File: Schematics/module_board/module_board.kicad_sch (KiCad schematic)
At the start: 33 parts, among them J1 Conn_01x01_Male, J11 Conn_01x01_Male, J12 Conn_01x01_Male, J13 Conn_01x01_Male, J14 Conn_01x01_Male, J15 Conn_01x01_Male, J16 Conn_01x01_Male, J17 Conn_01x01_Male, J2 Conn_01x01_Male, J3 Conn_01x01_Male, J4 Conn_01x01_Male, J5 Conn_01x06_Male, U1 RP2040, U2 W25Q16JVSSIQ, Y1 ABLS-12.000MHZ-B4-T

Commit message: Update project symbol table
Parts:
- removed U2: W25Q16JVSSIQ, Package_SO:SOIC-8_5.23x5.23mm_P1.27mm, symbol Merrick_Symbols_KiCad6:W25Q16JVSSIQ
- added U?: W25Q16JVSSIQ, symbol prototroller_symbols:W25Q16JVSSIQ
- J5: footprint Prototroller:Mag_Pogo_6P_P2.2mm_Male -> prototroller_footprints:Mag_Pogo_6P_P2.2mm_Male
- Y1: footprint ABLS-12:XTAL_ABLS-12.000MHZ-B4-T -> prototroller_footprints:XTAL_ABLS-12.000MHZ-B4-T
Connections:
- net +3V3: now also U?.8 (VCC)
- net GND: now also U?.4 (GND)
- net QSPI_NSS: now also U?.1 (~{CS})
- net QSPI_SCLK: now also U?.6 (CLK)
- net QSPI_SD0: now also U?.5 (DI(IO0))
- net QSPI_SD1: now also U?.2 (DO(IO1))
- net QSPI_SD2: now also U?.3 (IO2)
- net QSPI_SD3: now also U?.7 (IO3)
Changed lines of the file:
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@@
       (effects (font (size 1.27 1.27)) (justify right))
     )
-    (property "Footprint" "ABLS-12:XTAL_ABLS-12.000MHZ-B4-T" (id 2) (at 166.37 106.68 0)
+    (property "Footprint" "prototroller_footprints:XTAL_ABLS-12.000MHZ-B4-T" (id 2) (at 166.37 106.68 0)
       (effects (font (size 1.27 1.27)) hide)
     )
@@
     (pin "1")
   )
-  (symbol (lib_id "Merrick_Symbols_KiCad6:W25Q16JVSSIQ") (at 184.15 77.47 0) (unit 1)
-    (in_bom yes) (on_board yes)
-    (property "Reference" "U2" (id 0) (at 186.69 69.85 0)
-      (effects (font (size 1.27 1.27)) (justify left))
-    )
-    (property "Value" "W25Q16JVSSIQ" (id 1) (at 186.69 87.63 0)
-      (effects (font (size 1.27 1.27)) (justify left))
-    )
-    (property "Footprint" "Package_SO:SOIC-8_5.23x5.23mm_P1.27mm" (id 2) (at 158.75 80.01 0)
-      (effects (font (size 1.27 1.27)) hide)
-    )
-    (property "Datasheet" "" (id 3) (at 158.75 80.01 0)
-      (effects (font (size 1.27 1.27)) hide)
-    )
-    (pin "1")
-    (pin "2")
-    (pin "3")
-    (pin "4")
-    (pin "5")
-    (pin "6")
-    (pin "7")
-    (pin "8")
-  )
   (symbol (lib_id "Device:C") (at 106.68 41.91 0) (unit 1)
     (in_bom yes) (on_board yes) (fields_autoplaced)
@@
     (property "Reference" "J5" (id 0) (at 71.755 167.005 0))
     (property "Value" "Conn_01x06_Male" (id 1) (at 71.755 169.545 0))
-    (property "Footprint" "Prototroller:Mag_Pogo_6P_P2.2mm_Male" (id 2) (at 71.12 177.8 0)
+    (property "Footprint" "prototroller_footprints:Mag_Pogo_6P_P2.2mm_Male" (id 2) (at 71.12 177.8 0)
       (effects (font (size 1.27 1.27)) hide)
     )
@@
     (pin "2")
   )
+  (symbol (lib_id "prototroller_symbols:W25Q16JVSSIQ") (at 184.15 77.47 0) (unit 1)
+    (in_bom yes) (on_board yes) (fields_autoplaced)
+    (property "Reference" "U?" (id 0) (at 186.1694 66.04 0)
+      (effects (font (size 1.27 1.27)) (justify left))
+    )
+    (property "Value" "W25Q16JVSSIQ" (id 1) (at 186.1694 68.58 0)
+      (effects (font (size 1.27 1.27)) (justify left))
+    )
+    (property "Footprint" "" (id 2) (at 158.75 80.01 0)
+      (effects (font (size 1.27 1.27)) hide)
+    )
+    (property "Datasheet" "" (id 3) (at 158.75 80.01 0)
+      (effects (font (size 1.27 1.27)) hide)
+    )
+    (pin "1")
+    (pin "2")
+    (pin "3")
+    (pin "4")
+    (pin "5")
+    (pin "6")
+    (pin "7")
+    (pin "8")
+  )
   (symbol (lib_id "Device:C") (at 63.5 34.29 0) (unit 1)
     (in_bom yes) (on_board yes) (fields_autoplaced)
@@
     )
     (path "/7dd893ff-b49e-43fb-afd0-3a321ddb8ed6"
-      (reference "J5") (unit 1) (value "Conn_01x06_Male") (footprint "Prototroller:Mag_Pogo_6P_P2.2mm_Male")
+      (reference "J5") (unit 1) (value "Conn_01x06_Male") (footprint "prototroller_footprints:Mag_Pogo_6P_P2.2mm_Male")
     )
     (path "/64fe6c36-7f1f-48e1-a228-b6a618853dc6"
@@
       (reference "U1") (unit 1) (value "RP2040") (footprint "Package_DFN_QFN:QFN-56-1EP_7x7mm_P0.4mm_EP3.2x3.2mm")
     )
-    (path "/216ca7a2-00a8-4a6f-813d-3ef99867e82d"
-      (reference "U2") (unit 1) (value "W25Q16JVSSIQ") (footprint "Package_SO:SOIC-8_5.23x5.23mm_P1.27mm")
+    (path "/e3c130e0-31fd-409b-9bf2-42dc8cd4b75e"
+      (reference "U?") (unit 1) (value "W25Q16JVSSIQ") (footprint "")
     )
     (path "/039132b5-d1ff-4807-8a71-1bea6b495b8f"
-      (reference "Y1") (unit 1) (value "ABLS-12.000MHZ-B4-T") (footprint "ABLS-12:XTAL_ABLS-12.000MHZ-B4-T")
-    )
-  )
+      (reference "Y1") (unit 1) (value "ABLS-12.000MHZ-B4-T") (footprint "prototroller_footprints:XTAL_ABLS-12.000MHZ-B4-T")
+    )
+  )

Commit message: Module updates
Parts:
- removed J11, J12, J13, J14, J15, J16, J17: Conn_01x01_Male, Connector_Pin:Pin_D1.0mm_L10.0mm, symbol Connector:Conn_01x01_Male
- added J6, J7, J8, J9: Conn_01x02_Female, Connector_PinHeader_2.54mm:PinHeader_1x02_P2.54mm_Vertical, symbol Connector:Conn_01x02_Female
- U2: renamed from U?; footprint (none) -> Package_SO:SOIC-8_5.23x5.23mm_P1.27mm
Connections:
- net GPIO26_ADC0: now also J7.1 (Pin_1)
- net GPIO27_ADC1: now also J6.2 (Pin_2)
- net GPIO28_ADC2: now also J6.1 (Pin_1)
- net SPI1_CS_IO9: now also J8.1 (Pin_1)
- net SPI1_RX: now also J9.1 (Pin_1)
- net SPI1_SCK: now also J8.2 (Pin_2)
- net SPI1_TX: now also J9.2 (Pin_2)
- no-connect marks 21 -> 22

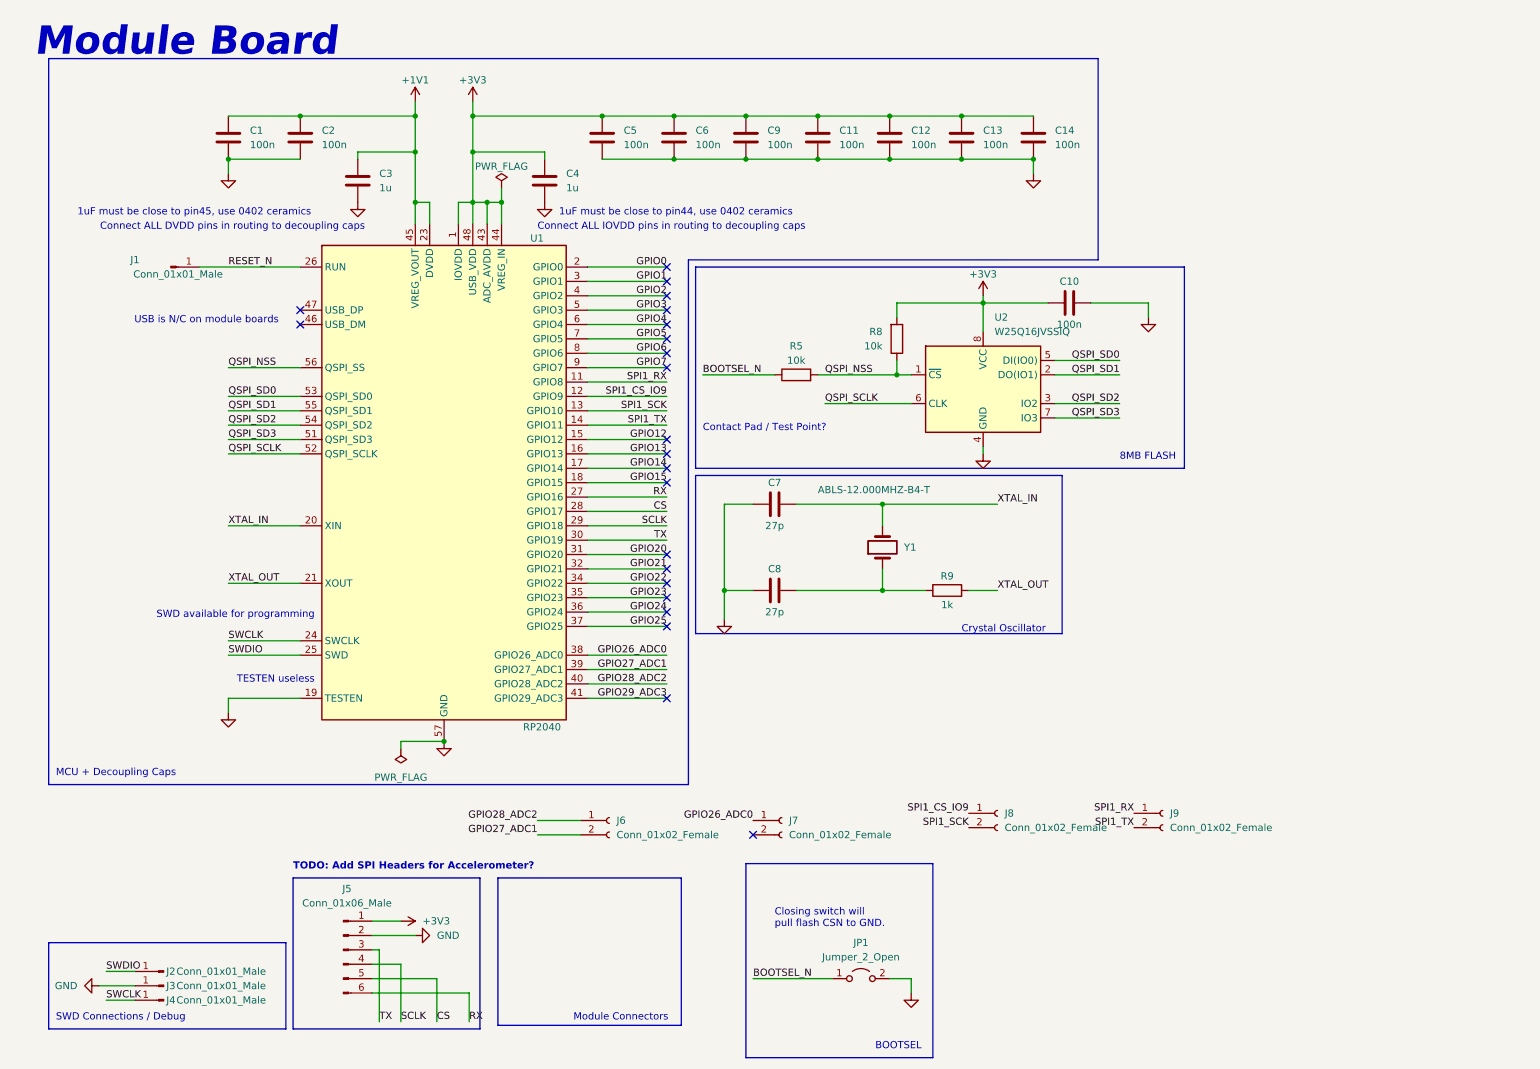
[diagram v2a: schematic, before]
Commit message: Added 2.54mm pitch male headers for SPI1 pins and ADC pins
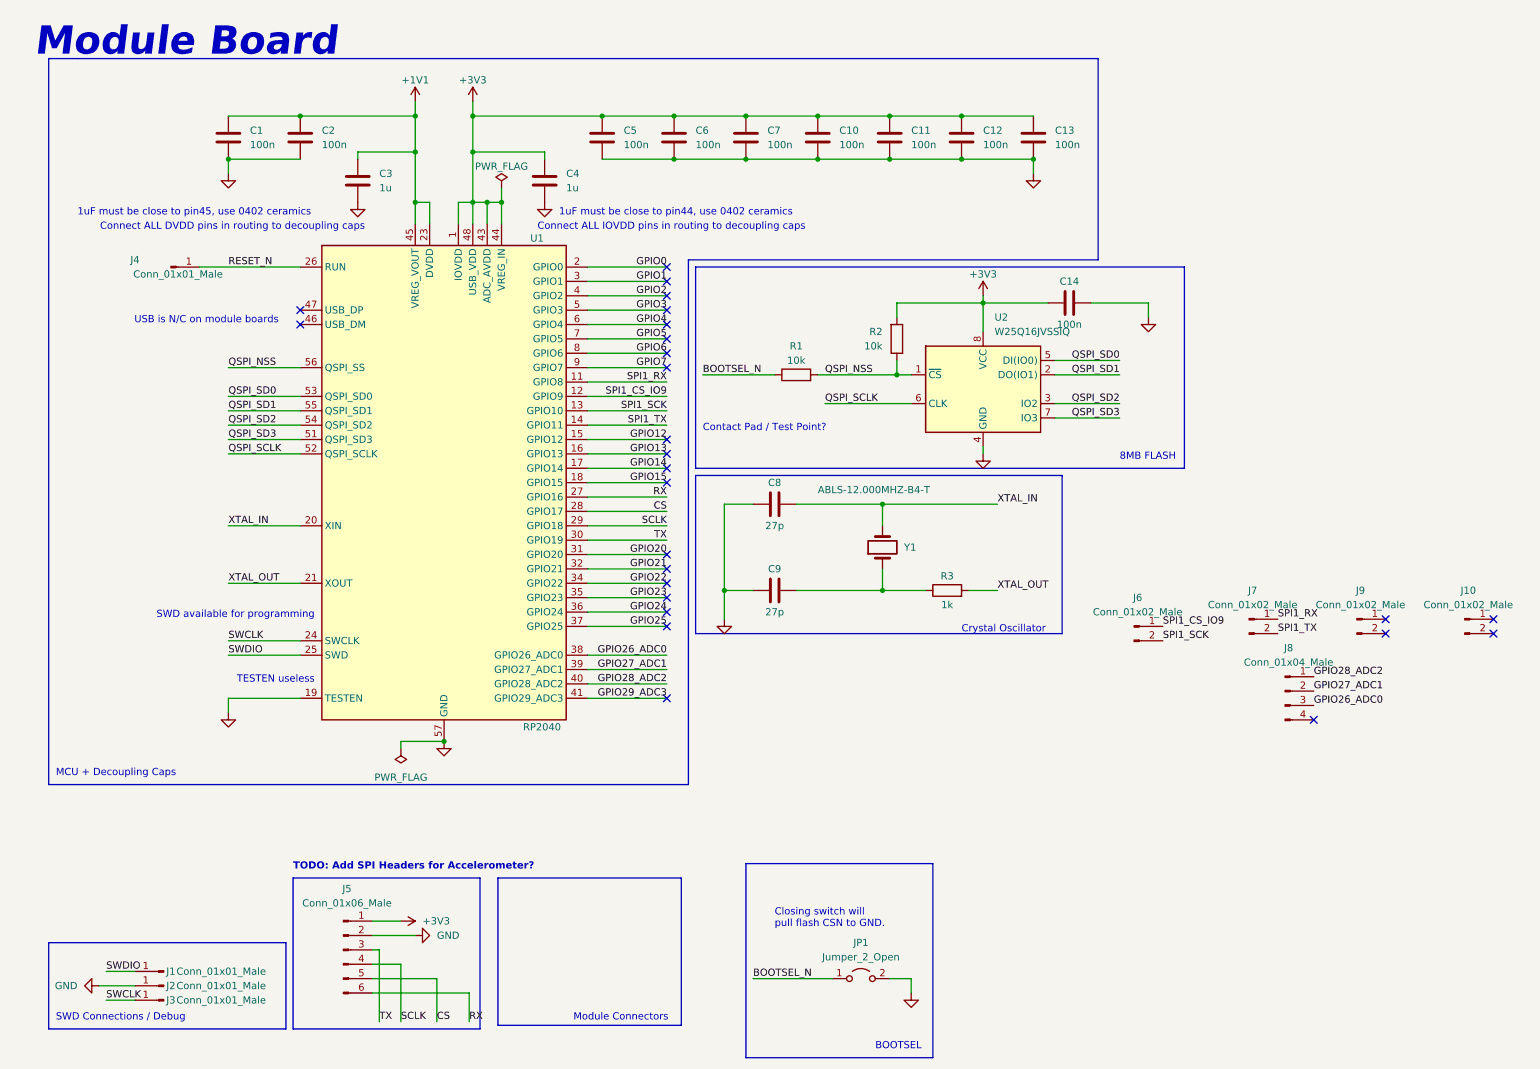
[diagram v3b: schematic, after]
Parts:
- removed J6, J7, J8, J9: Conn_01x02_Female, Connector_PinHeader_2.54mm:PinHeader_1x02_P2.54mm_Vertical, symbol Connector:Conn_01x02_Female
- added J10, J6, J7, J9: Conn_01x02_Male, Connector_PinHeader_2.54mm:PinHeader_1x02_P2.54mm_Vertical, symbol Connector:Conn_01x02_Male
- added J8: Conn_01x04_Male, Connector_PinHeader_2.54mm:PinHeader_1x04_P2.54mm_Vertical, symbol Connector:Conn_01x04_Male
- renumbered C11 to C10, C12 to C11, C13 to C12, C14 to C13, C10 to C14, C9 to C7, C7 to C8, C8 to C9, J2 to J1, J3 to J2, J4 to J3, J1 to J4, R5 to R1, R8 to R2, R9 to R3
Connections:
- net GPIO26_ADC0: now also J8.3 (Pin_3)
- net GPIO27_ADC1: now also J8.2 (Pin_2)
- net GPIO28_ADC2: now also J8.1 (Pin_1)
- net SPI1_CS_IO9: now also J6.1 (Pin_1)
- net SPI1_RX: now also J7.1 (Pin_1)
- net SPI1_SCK: now also J6.2 (Pin_2)
- net SPI1_TX: now also J7.2 (Pin_2)
- no-connect marks 22 -> 26

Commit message: Mod board finalizations
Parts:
- removed J1, J2, J3, J4: Conn_01x01_Male, TestPoint:TestPoint_Pad_D1.0mm, symbol Connector:Conn_01x01_Male
- added J1: Conn_01x04_Male, Connector_PinHeader_2.54mm:PinHeader_1x04_P2.54mm_Vertical, symbol Connector:Conn_01x04_Male
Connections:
- net GND: now also J1.1 (Pin_1)
- net GPIO25: now also J8.4 (Pin_4)
- net RESET_N: now also J1.2 (Pin_2)
- net SWCLK: now also J1.4 (Pin_4)
- net SWDIO: now also J1.3 (Pin_3)
- no-connect marks 26 -> 24
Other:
- note added: "CRYSTAL"
- note added: "INTERCONNECT"
- note added: "MCU"
- note added: "STRIPBOARD HEADERS"
- note added: "SWD HEADERS"
- note removed: "Crystal Oscillator"
- note removed: "MCU + Decoupling Caps"
- note removed: "Module Connectors"
- note removed: "SWD Connections / Debug"
- note removed: "TODO: Add SPI Headers for Accelerometer?"
- moved on the sheet: C1, C10, C11, C12, C13, C14, C2, C3, C4, C5, C6, C7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

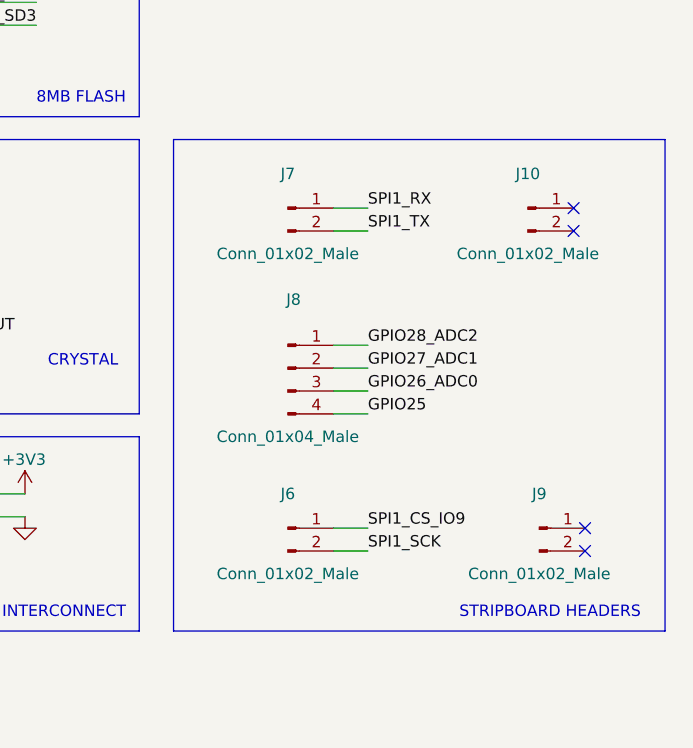
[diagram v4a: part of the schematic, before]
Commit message: improve clearance on module board edges
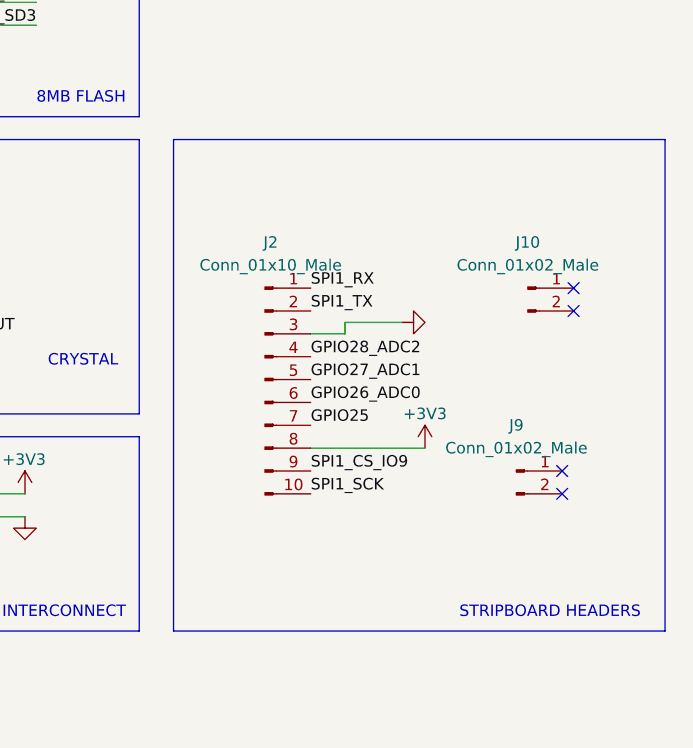
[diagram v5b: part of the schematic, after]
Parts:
- removed J6, J7: Conn_01x02_Male, Connector_PinHeader_2.54mm:PinHeader_1x02_P2.54mm_Vertical, symbol Connector:Conn_01x02_Male
- removed J8: Conn_01x04_Male, Connector_PinHeader_2.54mm:PinHeader_1x04_P2.54mm_Vertical, symbol Connector:Conn_01x04_Male
- added J2: Conn_01x10_Male, Connector_PinHeader_2.54mm:PinHeader_1x10_P2.54mm_Vertical, symbol Connector:Conn_01x10_Male
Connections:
- net +3V3: now also J2.8 (Pin_8)
- net GND: now also J2.3 (Pin_3)
- net GPIO25: now also J2.7 (Pin_7)
- net GPIO26_ADC0: now also J2.6 (Pin_6)
- net GPIO27_ADC1: now also J2.5 (Pin_5)
- net GPIO28_ADC2: now also J2.4 (Pin_4)
- net SPI1_CS_IO9: now also J2.9 (Pin_9)
- net SPI1_RX: now also J2.1 (Pin_1)
- net SPI1_SCK: now also J2.10 (Pin_10)
- net SPI1_TX: now also J2.2 (Pin_2)
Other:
- moved on the sheet: J10, J9
